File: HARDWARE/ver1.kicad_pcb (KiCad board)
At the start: 2 copper layers, 81.3 x 80.8 mm, 7 parts

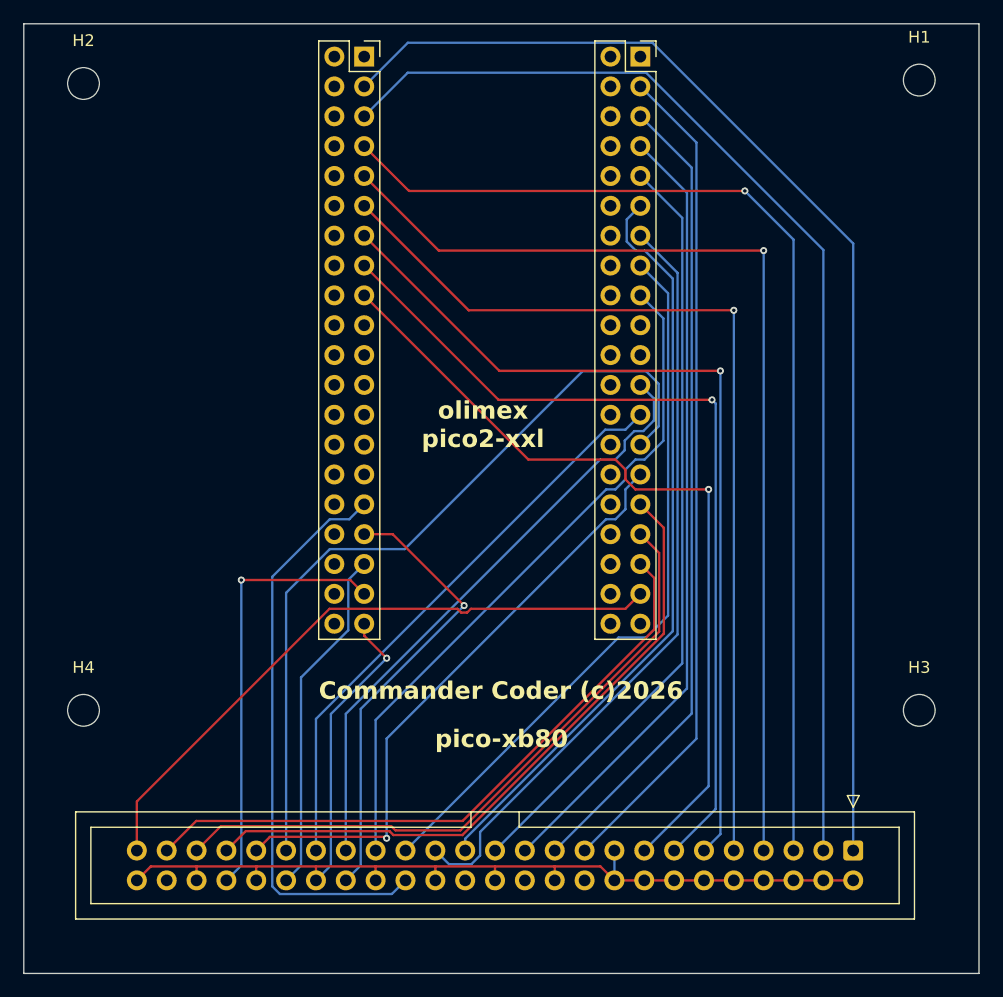
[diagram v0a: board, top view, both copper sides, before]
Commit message: Space the EXT headers to fit Olimex Rev B and Rev C, and clean up ERC
The Olimex RP2350-PICO2-XXL moved its EXT headers between revisions:
pin 1 to pin 1 is 23.54mm on Rev A/B and 22.86mm on Rev C. The sockets
were 23.50mm apart, which suits Rev B but leaves a Rev C 0.64mm out -
enough to bend pins. EXT2 now sits at 23.20mm, splitting the difference
so either revision is 0.34mm out. The sockets stay on F.Cu: the Olimex
plugs in face-up from above with its headers on its underside, so both
boards see pin 2 to the left of pin 1 and nothing is mirrored.

Address nets are renamed from the edge-connector pin they sit on (a1-a16)
to the Z80 signal they carry (A15-A0), matching the data nets, which
were already named by signal, and the firmware's PIN_A0 base. The
connections are unchanged.

The four unused edge-connector pins get their signal names - ~{INT} (b2),
~{M1} (b12), ~{HALT} (b14), RESET (b16) - while keeping their
no-connect flags until they're wired to the Pico.

Unused header pins get no-connect flags, and GND gets a PWR_FLAG, since
ground only arrives through connector pins (power comes to the Olimex
over USB) and ERC otherwise reports it undriven. ERC is now clean; DRC
leaves only the deliberate a/b pad renumbering on the XB80 footprint.

Adds a GND pour on both layers, and regenerates the Gerbers, drill
files, PDF and board render.

Co-Authored-By: Claude Opus 5.5 <noreply@anthropic.com>
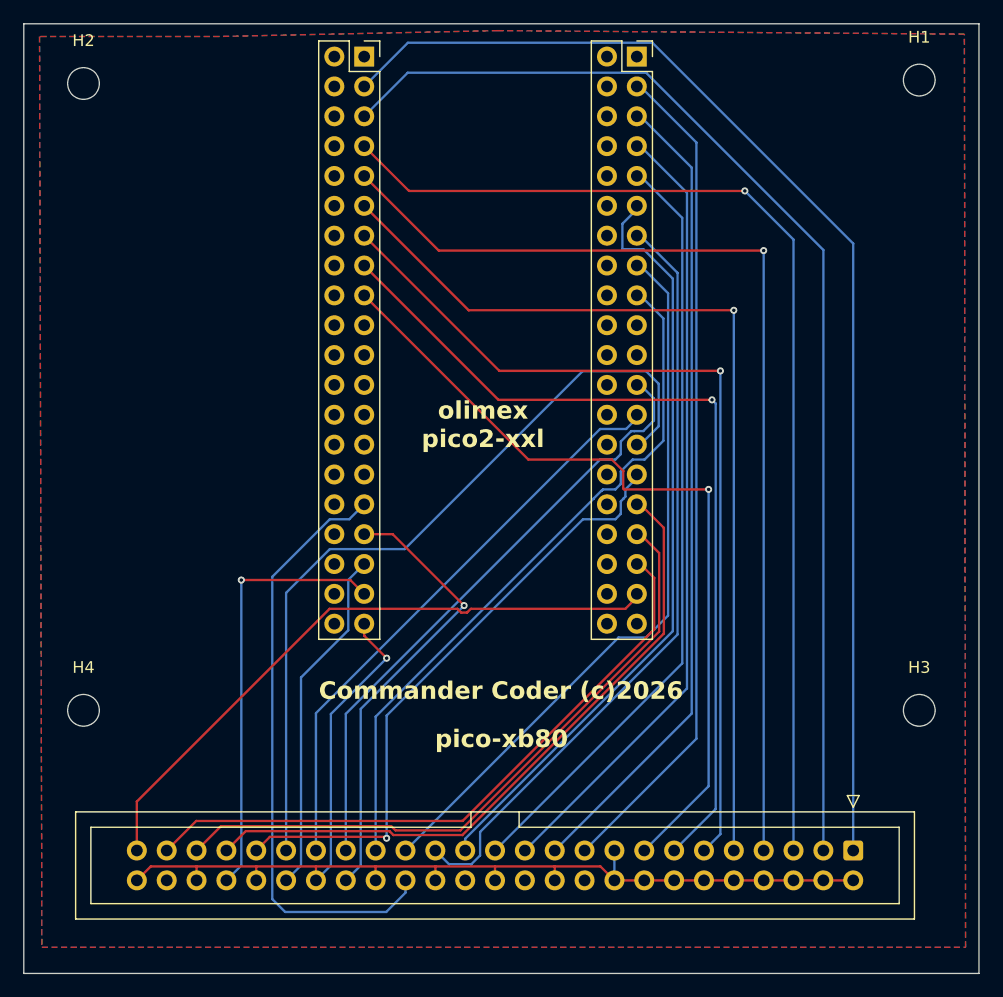
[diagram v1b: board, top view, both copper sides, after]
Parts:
- moved EXT2 0.30 mm to (125.8, 61.2)
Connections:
- net /A16 renamed /A0
- EXT1 pad 40: unconnected-(EXT1-Pin_40-Pad40) -> GND
- EXT2 pad 11: /A12 -> /A4
- EXT2 pad 13: /A11 -> /A5
- EXT2 pad 15: /A10 -> /A6
- EXT2 pad 17: /A9 -> /A7
- EXT2 pad 25: /A7 -> /A9
- EXT2 pad 27: /A6 -> /A10
- EXT2 pad 29: /A5 -> /A11
- EXT2 pad 31: /A4 -> /A12
- EXT2 pad 33: /A3 -> /A13
- EXT2 pad 35: /A2 -> /A14
- EXT2 pad 37: /A1 -> /A15
- EXT2 pad 39: unconnected-(EXT2-Pin_39-Pad39) -> GND
- EXT2 pad 40: unconnected-(EXT2-Pin_40-Pad40) -> GND
- EXT2 pad 5: /A15 -> /A1
- EXT2 pad 7: /A14 -> /A2
- EXT2 pad 9: /A13 -> /A3
- XB80 pad a1: /A1 -> /A15
- XB80 pad a10: /A10 -> /A6
- XB80 pad a11: /A11 -> /A5
- XB80 pad a12: /A12 -> /A4
- XB80 pad a13: /A13 -> /A3
- XB80 pad a14: /A14 -> /A2
- XB80 pad a15: /A15 -> /A1
- XB80 pad a2: /A2 -> /A14
- XB80 pad a3: /A3 -> /A13
- XB80 pad a4: /A4 -> /A12
- XB80 pad a5: /A5 -> /A11
- XB80 pad a6: /A6 -> /A10
- XB80 pad a7: /A7 -> /A9
- XB80 pad a9: /A9 -> /A7
- XB80 pad b12: unconnected-(XB80-Pin_b12-Padb12) -> /~{M1}
- XB80 pad b14: unconnected-(XB80-Pin_b14-Padb14) -> /~{HALT}
- XB80 pad b16: unconnected-(XB80-Pin_b16-Padb16) -> /RESET
- XB80 pad b2: unconnected-(XB80-Pin_b2-Padb2) -> /~{INT}
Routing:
- net /A15: track 69.1 -> 54.6 mm
- net /A1: track 54.6 -> 69.1 mm
- net /A5: track 52.0 -> 65.6 mm, vias 1 -> 0
- net /A11: track 65.6 -> 53.1 mm, vias 0 -> 1
- net /A2: track 55.3 -> 67.3 mm
- net /A14: track 67.3 -> 55.3 mm
- net /A7: track 49.5 -> 59.4 mm
- net /A9: track 59.1 -> 49.8 mm
- net /A3: track 56.3 -> 65.5 mm
- net /A13: track 65.5 -> 56.3 mm
- net /A4: track 57.0 -> 65.6 mm
- net /A12: track 64.7 -> 57.0 mm
- net /A6: track 67.7 -> 61.4 mm
- net /A10: track 61.4 -> 67.7 mm
- net /~{WR}: track 48.8 -> 51.3 mm
- added copper zone on B.Cu, net GND
- added copper zone on F.Cu, net GND
